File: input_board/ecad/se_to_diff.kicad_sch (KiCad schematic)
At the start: 16 parts, among them U4 MC33079, U5 NJM4580

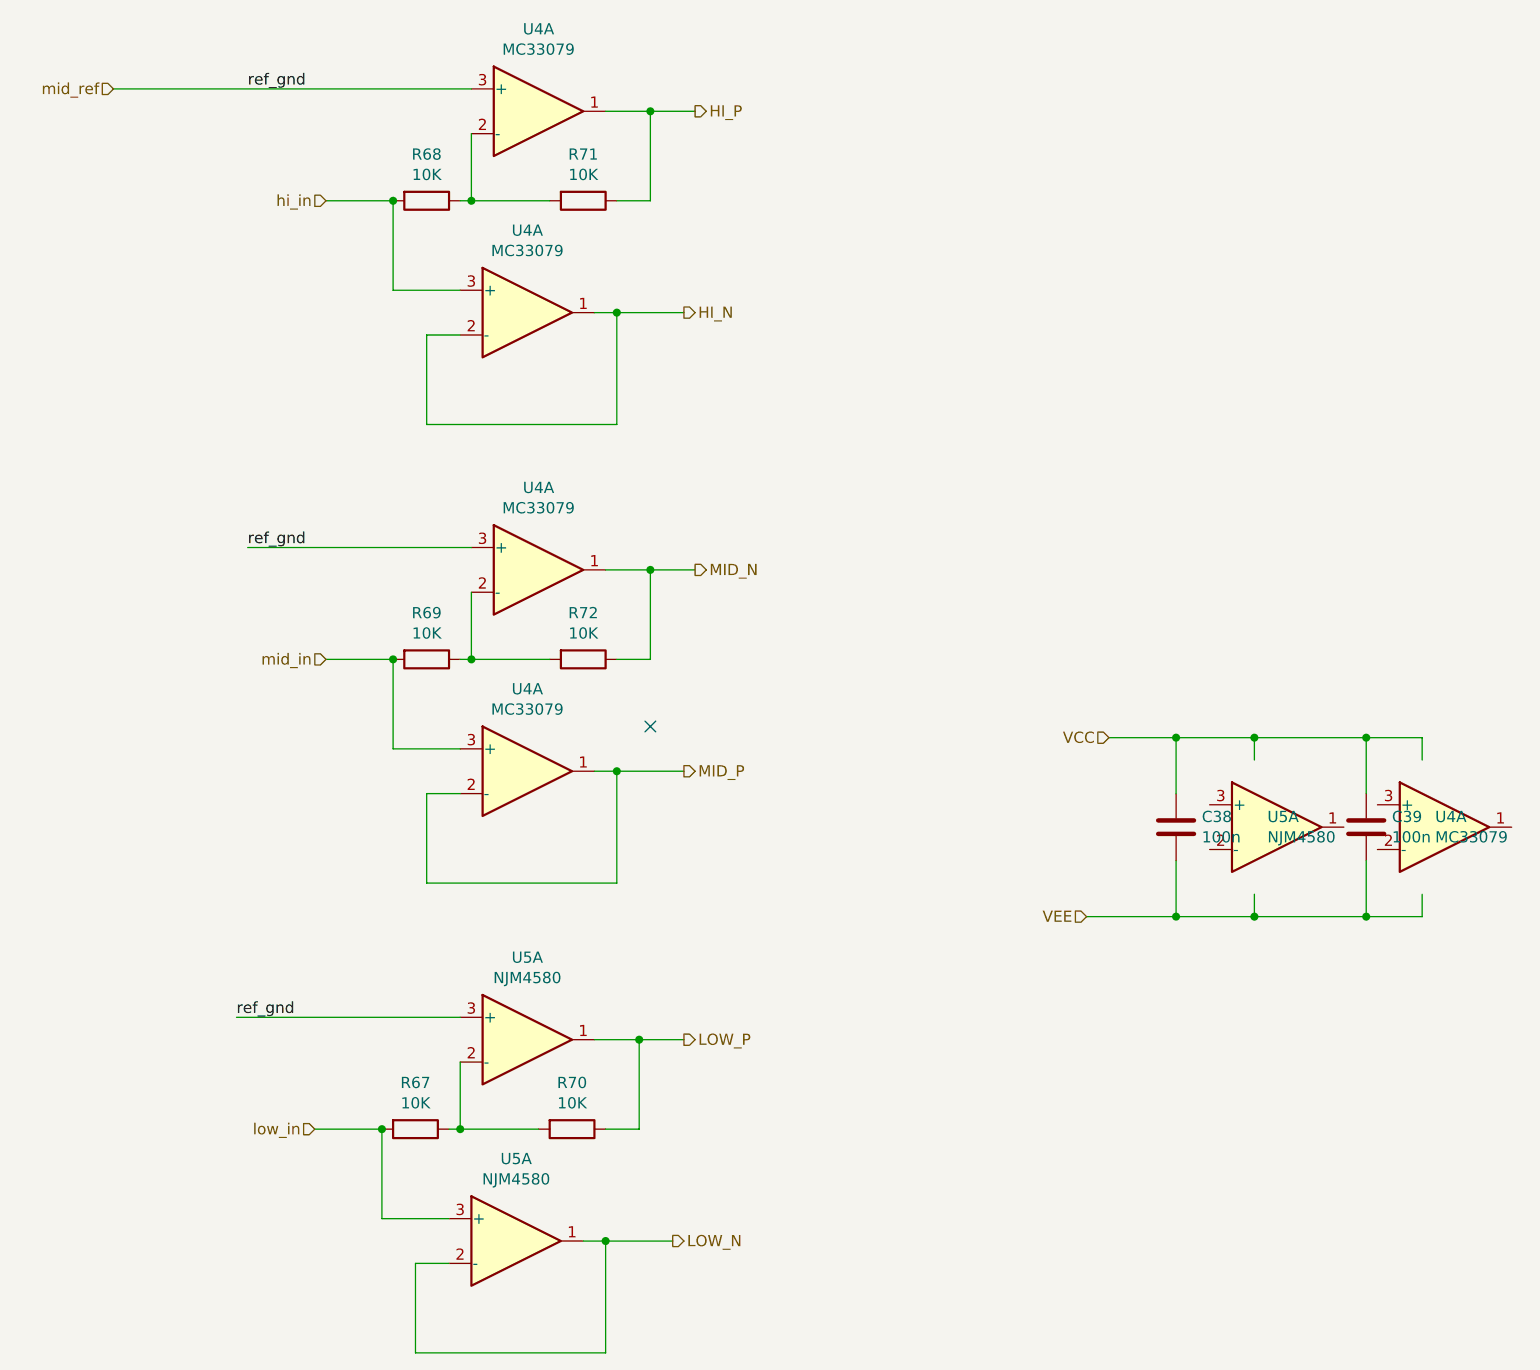
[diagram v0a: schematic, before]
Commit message: Input board: fix scematic and initial version of layout
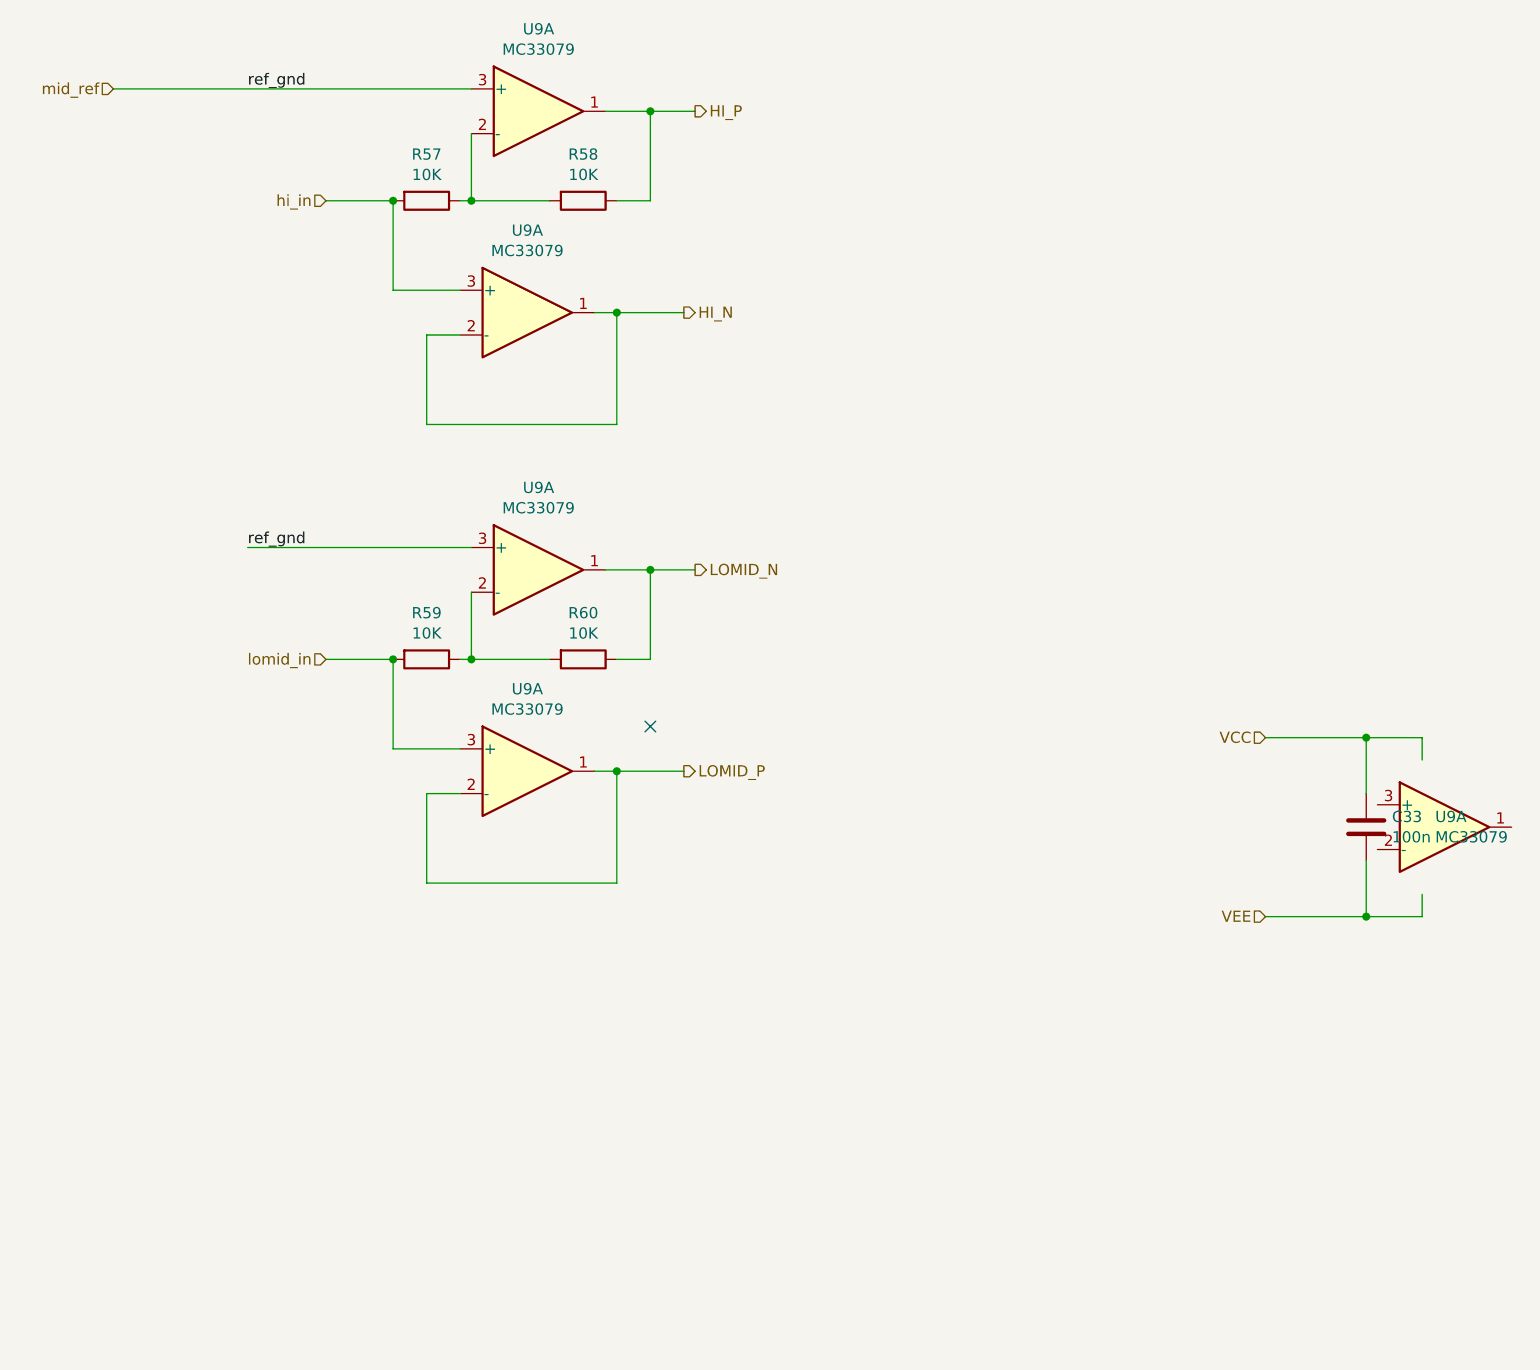
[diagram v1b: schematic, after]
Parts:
- removed C38: 100n, Capacitor_SMD:C_0805_2012Metric_Pad1.18x1.45mm_HandSolder, symbol Device:C
- removed R67, R70: 10K, Resistor_SMD:R_0805_2012Metric_Pad1.20x1.40mm_HandSolder, symbol Device:R
- removed U5 (x3): NJM4580, Package_SO:SOIC-8_3.9x4.9mm_P1.27mm, symbol Amplifier_Operational:NJM4580
- renumbered C39 to C33, R68 to R57, R71 to R58, R69 to R59, R72 to R60, U4 to U9
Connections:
- net MID_N renamed LOMID_N
- net MID_P renamed LOMID_P
- net mid_in renamed lomid_in
